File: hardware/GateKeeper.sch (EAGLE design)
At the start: 31 parts, among them K1 G3VM-351A, K2 G3VM-351A, U1 WEMOS-C3-PICO

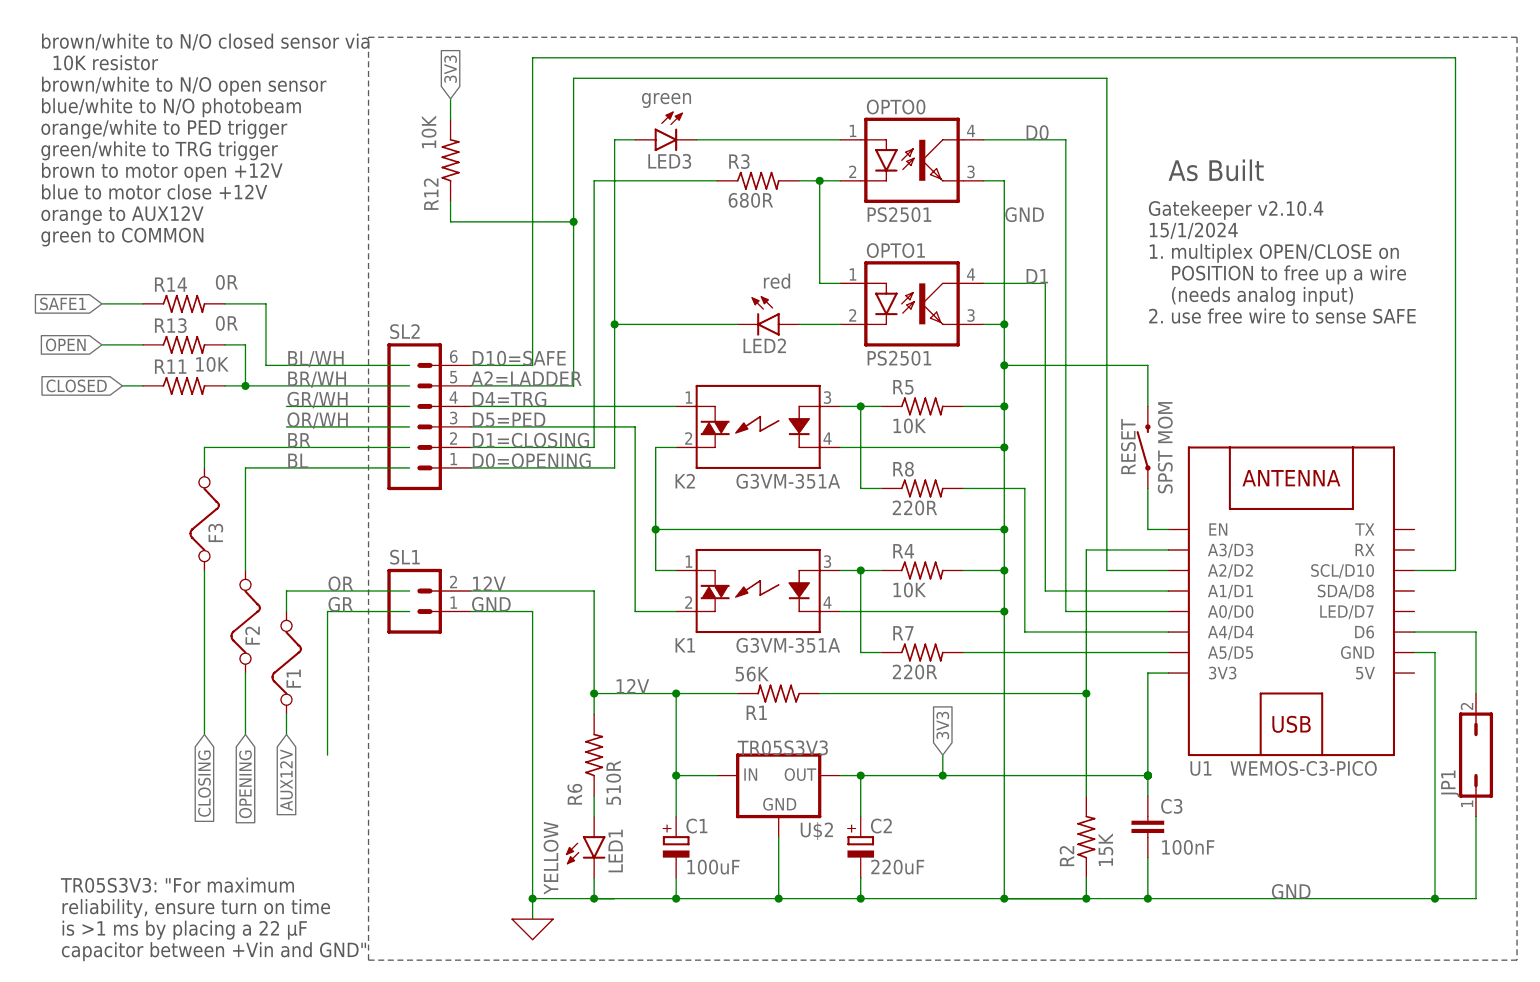
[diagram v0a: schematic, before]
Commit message: Revert to hardware version v2.10.1. Compared to v2.10.4 it has two digital inputs for the OPENED and CLOSED sensors, but does not support a SAFE sensor.
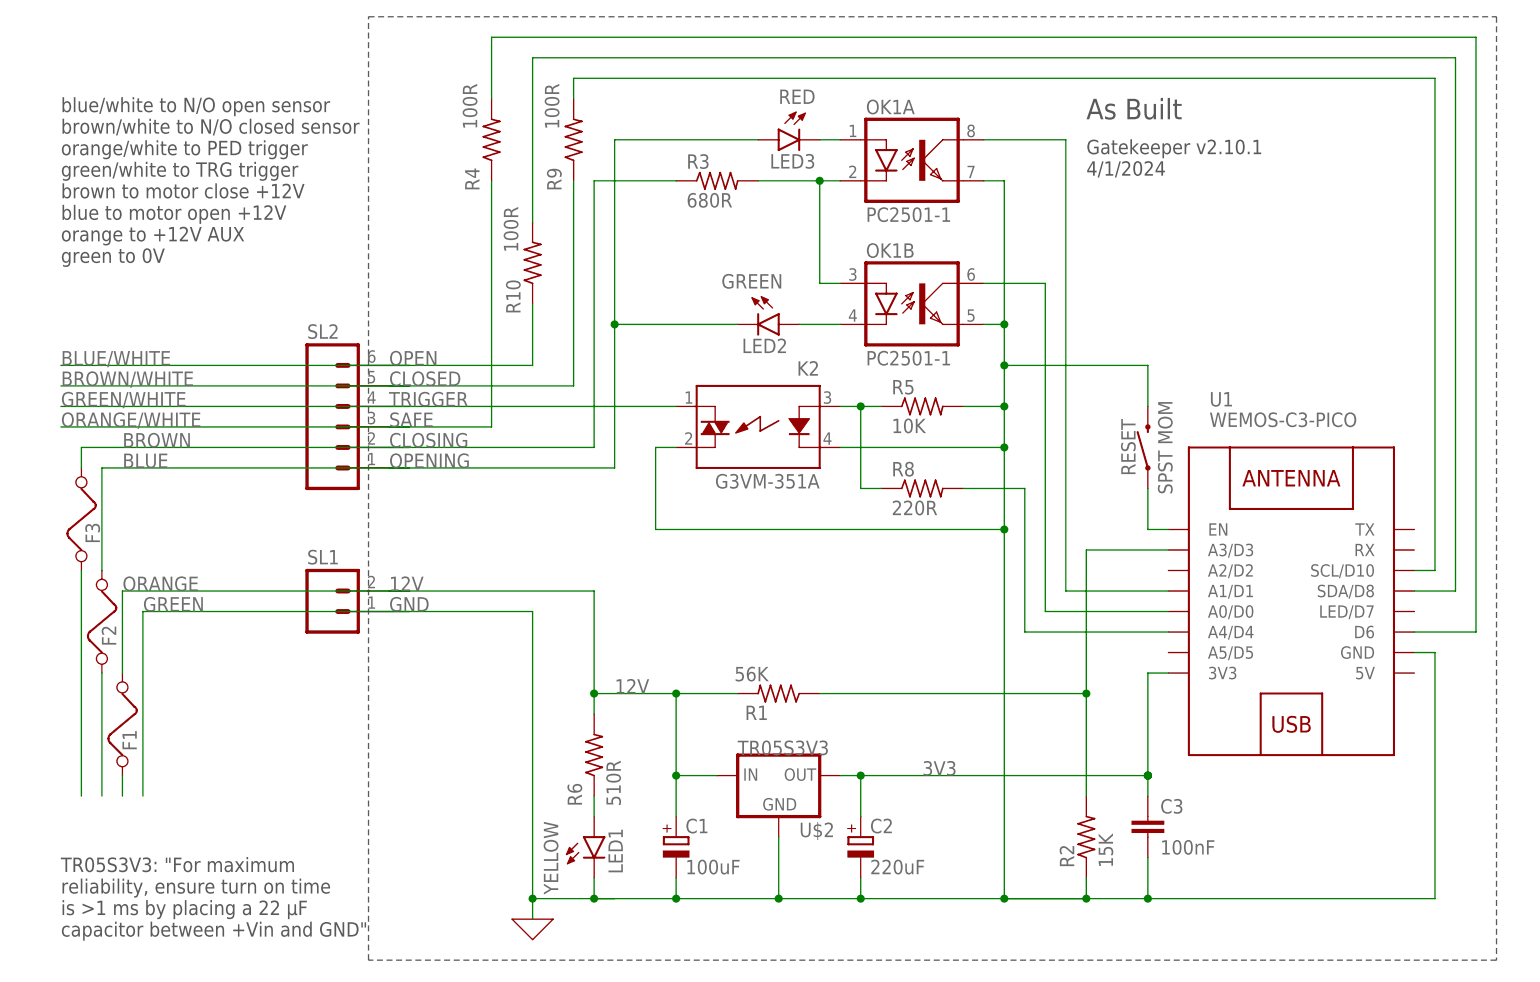
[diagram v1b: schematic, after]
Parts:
- removed JP1: (no value), jumper:JP1Q
- removed K1: G3VM-351A, relay:S202SE1
- removed OPTO0, OPTO1: PS2501, optocoupler:LTV816
- removed R11, R12: 10K, rcl:R-US_0207/10
- removed R13, R14: 0R, rcl:R-US_0207/10
- removed R7: 220R, rcl:R-US_0207/10
- added OK1: PC2501-1, optocoupler:PC827
- added R10, R9: 100R, rcl:R-US_0207/10
- LED2: value red -> GREEN
- LED3: value green -> RED
- R4: value 10K -> 100R
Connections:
- net AUX12V renamed N$5
- net BL renamed BLUE
- net BR renamed BROWN
- net D4=TRG renamed TRIGGER
- net OR renamed ORANGE
- removed net A2=LADDER: R12.1, SL2.5, U1.A2/D2
- removed net ANODE1: OPTO0.C, OPTO1.A, R3.2
- removed net BL/WH: R14.2
- removed net BR/WH: R11.2, R13.2
- removed net D0: OPTO0.COL, U1.A0/D0
- removed net D0=OPENING: LED2.C, LED3.A, SL2.1
- removed net D1: OPTO1.COL, U1.A1/D1
- removed net D10=SAFE: SL2.6, U1.SCL/D10
- removed net D1=CLOSING: R3.1, SL2.2
- removed net D5=PED: K1.DS2, SL2.3
- removed net N$16: K1.A, R4.1, R7.1
- removed net N$2: R7.2, U1.A5/D5
- removed net SAFE1: R14.1
- new net D6: R4.2, U1.D6
- new net N$11: F3.1
- new net N$21: OK1A.C, OK1B.A, R3.2
- new net N$4: LED3.C, OK1A.A
- new net N$8: F2.1
- new net SAFE: R4.1, SL2.3
- net 3V3: no longer R12.2
- net CLOSED: now also R9.1, R9.2, SL2.5, U1.SCL/D10; no longer R11.1
- net CLOSING: now also R3.1, SL2.2; no longer F3.1
- net GND: now also OK1A.EMIT, OK1B.EMIT; no longer JP1.1, K1.DS1, K1.K, OPTO0.EMIT, OPTO1.EMIT, R4.2
- net N$1: now also OK1B.C; no longer OPTO1.C
- net N$3: now also OK1B.COL, U1.A0/D0; no longer LED3.C, OPTO0.A
- net N$6: now also OK1A.COL, U1.A1/D1; no longer JP1.2, U1.D6
- net OPEN: now also R10.1, R10.2, SL2.6, U1.SDA/D8; no longer R13.1
- net OPENING: now also LED2.C, LED3.A, SL2.1; no longer F2.1
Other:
- note added: "Gatekeeper v2.10.1 4/1/2024"
- note added: "blue/white to N/O open sensor brown/white to N/O closed sensor orange/white to PED trigger green/white to TRG trigger brown to motor close +12V blue to motor open +12V orange to +12V AUX green to 0V"
- note removed: "Gatekeeper v2.10.4 15/1/2024 1. multiplex OPEN/CLOSE on POSITION to free up a wire (needs analog input) 2. use free wire to sense SAFE"
- note removed: "brown/white to N/O closed sensor via 10K resistor brown/white to N/O open sensor blue/white to N/O photobeam orange/white to PED trigger green/white to TRG trigger brown to motor open +12V blue to motor close +12V orange to AUX12V green to COMMON"
- moved on the sheet: F1, F2, F3, LED3, R3, R4, SL1, SL2

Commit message: Revert to hardware version 2.10.0. Compared to 2.10.1 this version has a pedestrian output but no "safe" input.
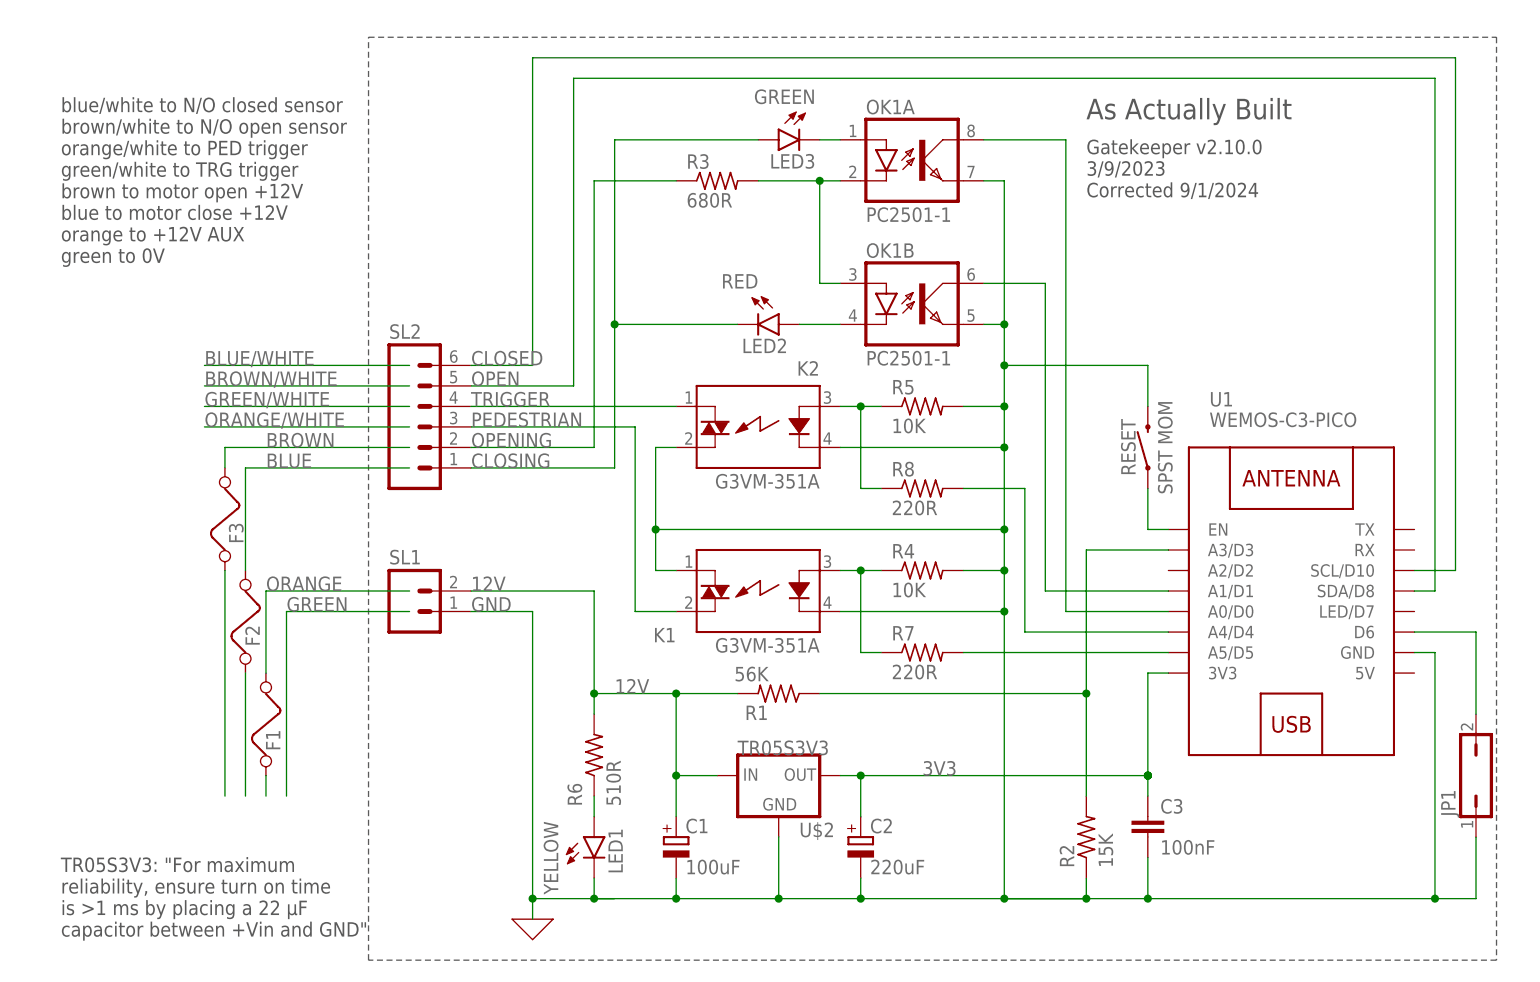
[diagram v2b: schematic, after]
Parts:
- removed R10, R9: 100R, rcl:R-US_0207/10
- added JP1: (no value), jumper:JP1Q
- added K1: G3VM-351A, relay:S202SE1
- added R7: 220R, rcl:R-US_0207/10
- LED2: value GREEN -> RED
- LED3: value RED -> GREEN
- R4: value 100R -> 10K
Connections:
- removed net D6: R4.2, U1.D6
- removed net SAFE: R4.1, SL2.3
- new net N$13: JP1.2, U1.D6
- new net N$16: K1.A, R4.1, R7.1
- new net N$2: R7.2, U1.A5/D5
- new net PEDESTRIAN: K1.DS2, SL2.3
- net CLOSED: now also SL2.6; no longer R9.1, R9.2, SL2.5
- net CLOSING: now also LED2.C, LED3.A, SL2.1; no longer R3.1, SL2.2
- net GND: now also JP1.1, K1.DS1, K1.K, R4.2
- net N$3: now also U1.A1/D1; no longer U1.A0/D0
- net N$6: now also U1.A0/D0; no longer U1.A1/D1
- net OPEN: now also SL2.5; no longer R10.1, R10.2, SL2.6
- net OPENING: now also R3.1, SL2.2; no longer LED2.C, LED3.A, SL2.1
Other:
- note added: "As Actually Built"
- note added: "Gatekeeper v2.10.0 3/9/2023 Corrected 9/1/2024"
- note added: "blue/white to N/O closed sensor brown/white to N/O open sensor orange/white to PED trigger green/white to TRG trigger brown to motor open +12V blue to motor close +12V orange to +12V AUX green to 0V"
- note removed: "As Built"
- note removed: "Gatekeeper v2.10.1 4/1/2024"
- note removed: "blue/white to N/O open sensor brown/white to N/O closed sensor orange/white to PED trigger green/white to TRG trigger brown to motor close +12V blue to motor open +12V orange to +12V AUX green to 0V"
- moved on the sheet: F1, F2, F3, R4, SL1, SL2
